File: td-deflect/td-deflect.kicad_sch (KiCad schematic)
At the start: 94 parts, among them J10 Conn_01x02_Male, J11 Conn_01x02_Male, Q1 BSZ42DN25NS3GATMA1, Q10 IPD50R380CE, Q11 IPD50R380CE, Q2 G3R450MT17J, Q3 BSZ42DN25NS3GATMA1, Q4 BCP56, Q5 BCP53, Q6 BD139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

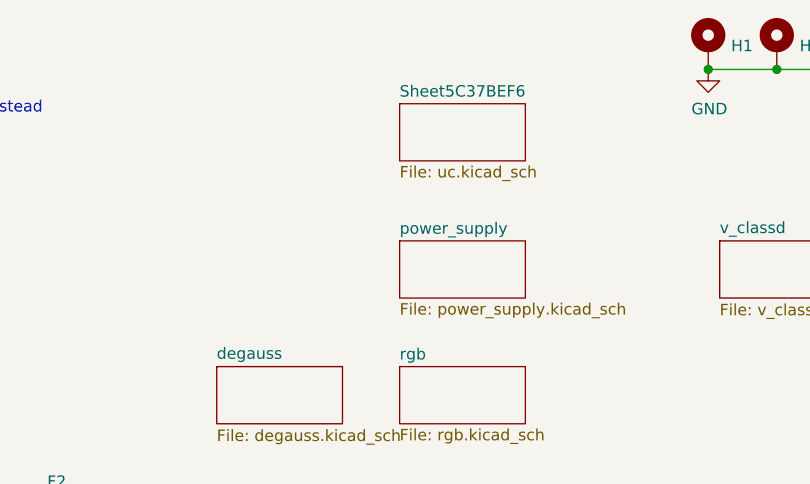
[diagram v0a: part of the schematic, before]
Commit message: update kicad format and move flyback to separate sheet
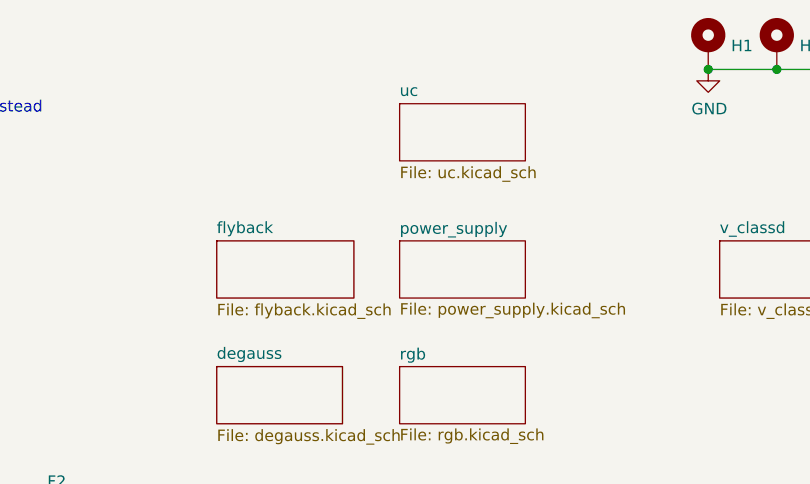
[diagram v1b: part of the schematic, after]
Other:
- sheet Sheet5C37BEF6 renamed uc
- added sheet flyback (flyback.kicad_sch)
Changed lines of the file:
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@@
-(kicad_sch (version 20221206) (generator eeschema)
+(kicad_sch (version 20230121) (generator eeschema)
   (paper "A4")
   (junction (at 35.56 160.02) (diameter 1.016) (color 0 0 0 0)
@@
     (stroke (width 0) (type solid))
     (fill (color 0 0 0 0.0000))
-    (property "Sheetname" "Sheet5C37BEF6" (at 217.17 28.5745 0)
+    (property "Sheetname" "uc" (at 217.17 28.4984 0)
       (effects (font (size 1.27 1.27)) (justify left bottom))
     )
-    (property "Sheetfile" "uc.kicad_sch" (at 217.17 36.0685 0)
+    (property "Sheetfile" "uc.kicad_sch" (at 217.17 36.1446 0)
       (effects (font (size 1.27 1.27)) (justify left top))
     )
@@
       )
     )
+  )
+  (sheet (at 196.85 44.45) (size 15.24 6.35) (fields_autoplaced)
+    (stroke (width 0.1524) (type solid))
+    (fill (color 0 0 0 0.0000))
+    (property "Sheetname" "flyback" (at 196.85 43.7384 0)
+      (effects (font (size 1.27 1.27)) (justify left bottom))
+    )
+    (property "Sheetfile" "flyback.kicad_sch" (at 196.85 51.3846 0)
+      (effects (font (size 1.27 1.27)) (justify left top))
+    )
+    (property "Field2" "" (at 196.85 44.45 0)
+      (effects (font (size 1.27 1.27)) hide)
+    )
+    (instances
+      (project "td-deflect"
+        (path "/55a1a5e1-4d11-4c3e-b2b4-b9d50ddc5f9d" (page "7"))
+      )
+    )

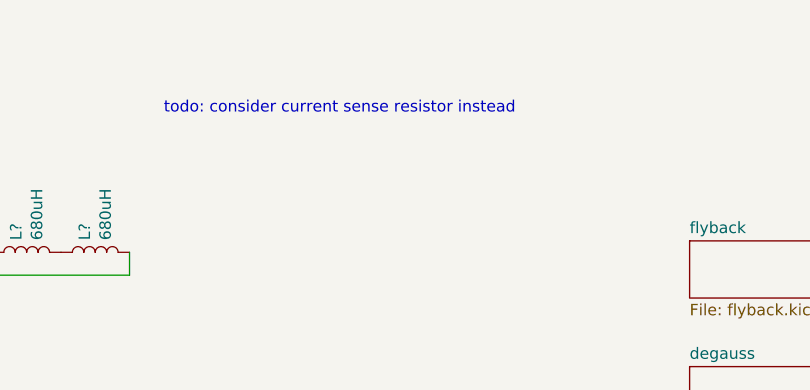
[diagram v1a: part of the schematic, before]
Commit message: drop current sense note
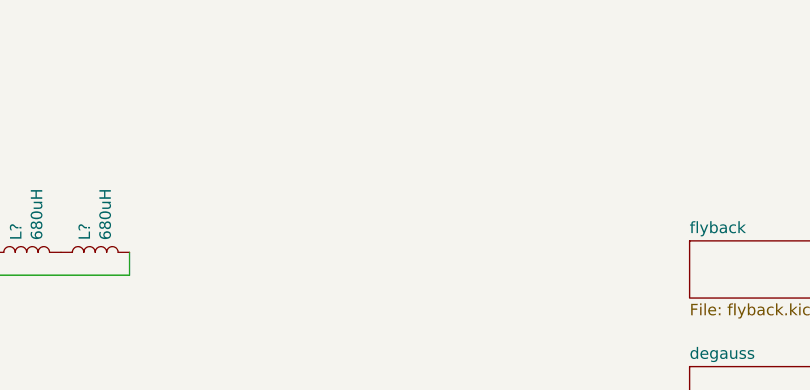
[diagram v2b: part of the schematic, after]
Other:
- note removed: "todo: consider current sense resistor instead"
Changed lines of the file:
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@@
-    (effects (font (size 1.27 1.27)) (justify left bottom))
-  )
-  (text "todo: consider current sense resistor instead" (at 138.43 30.48 0)
     (effects (font (size 1.27 1.27)) (justify left bottom))
   )

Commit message: more updates
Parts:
- added TP1, TP2, TP3: TestPoint, TestPoint:TestPoint_Keystone_5010-5014_Multipurpose, symbol Connector:TestPoint
- C59: renamed from C?; footprint (none) -> Capacitor_SMD:C_0805_2012Metric_Pad1.15x1.40mm_HandSolder
- C69: renamed from C?; footprint (none) -> Capacitor_SMD:CP_Elec_8x11.9; symbol Device:C -> Device:C_Polarized; Digikey (none) -> 493-4571-1-ND
- R67, R68, R70, R71: renamed from R?; footprint (none) -> Resistor_SMD:R_0805_2012Metric_Pad1.15x1.40mm_HandSolder
- gave numbers to parts that had none: 20
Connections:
- net HOT_CURRENT: now also TP2.1
- net HOT_VOLTAGE: now also TP1.1
- net V_CURRENT: now also TP3.1

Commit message: even more updates
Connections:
- net GND: no longer Q2.2 (DS)
- net HOT_CURRENT: now also Q2.2 (DS)
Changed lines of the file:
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@@
   (junction (at 251.46 25.4) (diameter 1.016) (color 0 0 0 0)
   )
-  (junction (at 68.58 88.9) (diameter 0) (color 0 0 0 0)
-  )
   (junction (at 266.7 25.4) (diameter 1.016) (color 0 0 0 0)
   )
@@
   (junction (at 228.6 93.98) (diameter 1.016) (color 0 0 0 0)
   )
+  (junction (at 81.28 86.36) (diameter 0) (color 0 0 0 0)
+  )
   (junction (at 62.23 162.56) (diameter 1.016) (color 0 0 0 0)
   )
@@
     (stroke (width 0) (type solid))
   )
+  (wire (pts (xy 78.74 86.36) (xy 81.28 86.36))
+    (stroke (width 0) (type default))
+  )
   (wire (pts (xy 228.6 93.98) (xy 232.41 93.98))
     (stroke (width 0) (type solid))
@@
     (stroke (width 0) (type solid))
   )
-  (wire (pts (xy 78.74 83.82) (xy 78.74 88.9))
-    (stroke (width 0) (type default))
-  )
   (wire (pts (xy 54.61 170.18) (xy 39.37 170.18))
     (stroke (width 0) (type solid))
@@
     (stroke (width 0) (type solid))
   )
+  (wire (pts (xy 78.74 83.82) (xy 78.74 86.36))
+    (stroke (width 0) (type default))
+  )
   (wire (pts (xy 248.92 93.98) (xy 248.92 119.38))
     (stroke (width 0) (type default))
@@
     (stroke (width 0) (type solid))
   )
-  (wire (pts (xy 78.74 88.9) (xy 68.58 88.9))
-    (stroke (width 0) (type default))
-  )
   (wire (pts (xy 246.38 93.98) (xy 246.38 92.71))

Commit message: small bugfix
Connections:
- net +3V3: no longer R1.1
- new net +3.3VA: R1.1
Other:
- note added: "check output voltage limits"
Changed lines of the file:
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@@
     (stroke (width 0) (type solid))
   )
+  (wire (pts (xy 54.61 149.86) (xy 54.61 162.56))
+    (stroke (width 0) (type solid))
+  )
   (wire (pts (xy 220.98 88.9) (xy 220.98 111.76))
     (stroke (width 0) (type solid))
@@
     (effects (font (size 1.27 1.27)) (justify left bottom))
   )
+  (text "check output voltage limits" (at 95.25 177.8 0)
+    (effects (font (size 1.27 1.27)) (justify left bottom))
+  )
   (text "todo: cooling?" (at 185.42 133.35 0)
     (effects (font (size 1.27 1.27)) (justify left bottom))
@@
     (effects (font (size 1.27 1.27)) (justify left bottom))
   )
-  (label "virtual_ground" (at 273.05 129.54 0) (fields_autoplaced)
-    (effects (font (size 1.27 1.27)) (justify left bottom))
-  )
   (global_label "HOT_IN" (shape input) (at 44.45 81.28 180) (fields_autoplaced)
     (effects (font (size 1.27 1.27)) (justify right))
@@
     )
   )
-  (global_label "virtual_ground" (shape input) (at 54.61 149.86 180) (fields_autoplaced)
-    (effects (font (size 1.27 1.27)) (justify right))
-    (property "Intersheetrefs" "${INTERSHEET_REFS}" (at 38.7391 149.9394 0)
-      (effects (font (size 1.27 1.27)) (justify right) hide)
+  (global_label "virtual_ground" (shape input) (at 273.05 129.54 0) (fields_autoplaced)
+    (effects (font (size 1.27 1.27)) (justify left))
+    (property "Intersheetrefs" "${INTERSHEET_REFS}" (at 288.9209 129.4606 0)
+      (effects (font (size 1.27 1.27)) (justify left) hide)
     )
   )
@@
     )
   )
-  (symbol (lib_id "power:+3.3V") (at 35.56 152.4 0) (unit 1)
-    (in_bom yes) (on_board yes) (dnp no)
-    (property "Reference" "#PWR0159" (at 35.56 156.21 0)
-      (effects (font (size 1.27 1.27)) hide)
-    )
-    (property "Value" "+3.3V" (at 35.941 148.0058 0)
-      (effects (font (size 1.27 1.27)))
-    )
-    (property "Footprint" "" (at 35.56 152.4 0)
-      (effects (font (size 1.27 1.27)) hide)
-    )
-    (property "Datasheet" "" (at 35.56 152.4 0)
-      (effects (font (size 1.27 1.27)) hide)
-    )
-    (pin "1")
-    (instances
-      (project "td-deflect"
-        (path "/55a1a5e1-4d11-4c3e-b2b4-b9d50ddc5f9d"
-          (reference "#PWR0159") (unit 1)
-        )
-      )
-    )
-  )
   (symbol (lib_id "Device:R") (at 54.61 146.05 0) (unit 1)
     (in_bom yes) (on_board yes) (dnp no)
@@
         )
       )
+    )
+  )
+  (symbol (lib_id "power:+3.3VA") (at 35.56 152.4 0) (unit 1)
+    (in_bom yes) (on_board yes) (dnp no) (fields_autoplaced)
+    (property "Reference" "#PWR010" (at 35.56 156.21 0)
+      (effects (font (size 1.27 1.27)) hide)
+    )
+    (property "Value" "+3.3VA" (at 35.56 148.8981 0)
+      (effects (font (size 1.27 1.27)))
+    )
+    (property "Footprint" "" (at 35.56 152.4 0)
+      (effects (font (size 1.27 1.27)) hide)
+    )
+    (property "Datasheet" "" (at 35.56 152.4 0)
+      (effects (font (size 1.27 1.27)) hide)
+    )
+    (pin "1")
+    (instances
+      (project "td-deflect"
+        (path "/55a1a5e1-4d11-4c3e-b2b4-b9d50ddc5f9d/00000000-0000-0000-0000-00005c37bef7"
+          (reference "#PWR010") (unit 1)
+        )
+        (path "/55a1a5e1-4d11-4c3e-b2b4-b9d50ddc5f9d"
+          (reference "#PWR045") (unit 1)
+        )
+      )

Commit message: switch to new 0805 footprint
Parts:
- C1, C10, C12, C2, C3, C4, C5, C59, C60, C68, C7, C8, C9: footprint Capacitor_SMD:C_0805_2012Metric_Pad1.15x1.40mm_HandSolder -> Capacitor_SMD:C_0805_2012Metric_Pad1.18x1.45mm_HandSolder
- R1, R10, R11, R15, R16, R17, R18, R2, R20, R21, R3, R4, R5, R64, R65, R67, R68, R7, R70, R71, R72, R8, R9: footprint Resistor_SMD:R_0805_2012Metric_Pad1.15x1.40mm_HandSolder -> Resistor_SMD:R_0805_2012Metric_Pad1.20x1.40mm_HandSolder
- R23, R24, R25, R26, R27, R28: footprint Resistor_SMD:R_1206_3216Metric_Pad1.42x1.75mm_HandSolder -> Resistor_SMD:R_1206_3216Metric_Pad1.30x1.75mm_HandSolder

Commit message: use off board bplus h supply
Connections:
- net HT: no longer Q1.5 (D)
- new net +3.3V: Q1.5 (D)
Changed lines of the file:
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@@
     (stroke (width 0) (type default))
   )
-  (wire (pts (xy 87.63 30.48) (xy 87.63 28.575))
+  (wire (pts (xy 87.63 27.94) (xy 87.63 30.48))
     (stroke (width 0) (type solid))
   )
@@
     )
   )
-  (symbol (lib_id "power:HT") (at 87.63 28.575 0) (unit 1)
-    (in_bom yes) (on_board yes) (dnp no)
-    (property "Reference" "#PWR0123" (at 87.63 25.527 0)
-      (effects (font (size 1.27 1.27)) hide)
-    )
-    (property "Value" "HT" (at 88.138 24.9428 0)
-      (effects (font (size 1.27 1.27)))
-    )
-    (property "Footprint" "" (at 87.63 28.575 0)
-      (effects (font (size 1.27 1.27)) hide)
-    )
-    (property "Datasheet" "" (at 87.63 28.575 0)
-      (effects (font (size 1.27 1.27)) hide)
-    )
-    (pin "1")
-    (instances
-      (project "td-deflect"
-        (path "/55a1a5e1-4d11-4c3e-b2b4-b9d50ddc5f9d"
-          (reference "#PWR0123") (unit 1)
-        )
-      )
-    )
-  )
   (symbol (lib_id "power:GND") (at 87.63 55.88 0) (unit 1)
     (in_bom yes) (on_board yes) (dnp no)
@@
         )
       )
+    )
+  )
+  (symbol (lib_id "td-crt:B+H") (at 87.63 27.94 0) (unit 1)
+    (in_bom yes) (on_board yes) (dnp no) (fields_autoplaced)
+    (property "Reference" "#PWR010" (at 87.63 31.75 0)
+      (effects (font (size 1.27 1.27)) hide)
+    )
+    (property "Value" "B+H" (at 87.63 23.8069 0)
+      (effects (font (size 1.27 1.27)))
+    )
+    (property "Footprint" "" (at 87.63 27.94 0)
+      (effects (font (size 1.27 1.27)) hide)
+    )
+    (property "Datasheet" "" (at 87.63 27.94 0)
+      (effects (font (size 1.27 1.27)) hide)
+    )
+    (pin "1")
+    (instances
+      (project "td-deflect"
+        (path "/55a1a5e1-4d11-4c3e-b2b4-b9d50ddc5f9d"
+          (reference "#PWR010") (unit 1)
+        )
+      )

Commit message: update part numbers
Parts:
- C59: value C -> 0.1uF; Digikey (none) -> 445-8899-1-ND
- Q1, Q3: value BSZ42DN25NS3GATMA1 -> BSC600N25NS3GATMA1CT-ND; Digikey BSZ42DN25NS3GATMA1CT-ND -> BSC600N25NS3GATMA1CT-ND
- Q6: value BD139 -> 2SC4382; Digikey 497-12750-5-ND -> 2SC4382-ND
- Q7: value BD140 -> 2SA1668; Digikey 497-14760-5-ND -> 2SA1668-ND
- U31: Digikey (none) -> 445-8899-1-ND
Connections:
- net HT is gone; now on net +3.3V: C59.1
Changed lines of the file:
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@@
       (effects (font (size 1.27 1.27)) (justify left))
     )
-    (property "Value" "BD140" (at 148.3868 136.017 0)
+    (property "Value" "2SA1668" (at 148.3868 136.017 0)
       (effects (font (size 1.27 1.27)) (justify left))
     )
@@
       (effects (font (size 1.27 1.27)) (justify left) hide)
     )
-    (property "Digikey" " 497-14760-5-ND " (at 143.51 137.16 0)
+    (property "Digikey" "2SA1668-ND" (at 143.51 137.16 0)
       (effects (font (size 1.27 1.27)) hide)
     )
@@
       (effects (font (size 1.27 1.27)) (justify left))
     )
-    (property "Value" "BD139" (at 148.3868 173.863 0)
+    (property "Value" "2SC4382" (at 148.3868 173.863 0)
       (effects (font (size 1.27 1.27)) (justify left))
     )
@@
       (effects (font (size 1.27 1.27)) (justify left) hide)
     )
-    (property "Digikey" " 497-12750-5-ND " (at 143.51 172.72 0)
+    (property "Digikey" "2SC4382-ND" (at 143.51 172.72 0)
       (effects (font (size 1.27 1.27)) hide)
     )
@@
       (effects (font (size 1.27 1.27)) (justify left))
     )
-    (property "Value" "BSZ42DN25NS3GATMA1" (at 90.2716 36.703 0)
+    (property "Value" "BSC600N25NS3GATMA1CT-ND" (at 90.2716 36.703 0)
       (effects (font (size 1.27 1.27)) (justify left))
     )
@@
       (effects (font (size 1.27 1.27)) (justify left) hide)
     )
-    (property "Digikey" "BSZ42DN25NS3GATMA1CT-ND" (at 85.09 35.56 0)
+    (property "Digikey" "BSC600N25NS3GATMA1CT-ND" (at 85.09 35.56 0)
       (effects (font (size 1.27 1.27)) hide)
     )
@@
       (effects (font (size 1.27 1.27)) (justify left))
     )
-    (property "Value" "BSZ42DN25NS3GATMA1" (at 90.2716 51.943 0)
+    (property "Value" "BSC600N25NS3GATMA1CT-ND" (at 90.2716 51.943 0)
       (effects (font (size 1.27 1.27)) (justify left))
     )
@@
       (effects (font (size 1.27 1.27)) (justify left) hide)
     )
-    (property "Digikey" "BSZ42DN25NS3GATMA1CT-ND" (at 85.09 50.8 0)
+    (property "Digikey" "BSC600N25NS3GATMA1CT-ND" (at 85.09 50.8 0)
       (effects (font (size 1.27 1.27)) hide)
     )
@@
     (property "Datasheet" "https://docs.broadcom.com/docs/AV02-0173EN" (at 191.77 147.32 0)
       (effects (font (size 1.27 1.27)) (justify left) hide)
+    )
+    (property "Digikey" "445-8899-1-ND" (at 191.77 147.32 90)
+      (effects (font (size 1.27 1.27)) hide)
     )
     (pin "1")
@@
     )
   )
-  (symbol (lib_id "power:HT") (at 26.67 39.37 0) (unit 1)
-    (in_bom yes) (on_board yes) (dnp no)
-    (property "Reference" "#PWR0160" (at 26.67 36.322 0)
-      (effects (font (size 1.27 1.27)) hide)
-    )
-    (property "Value" "HT" (at 27.178 35.7378 0)
-      (effects (font (size 1.27 1.27)))
-    )
-    (property "Footprint" "" (at 26.67 39.37 0)
-      (effects (font (size 1.27 1.27)) hide)
-    )
-    (property "Datasheet" "" (at 26.67 39.37 0)
-      (effects (font (size 1.27 1.27)) hide)
-    )
-    (pin "1")
-    (instances
-      (project "td-deflect"
-        (path "/55a1a5e1-4d11-4c3e-b2b4-b9d50ddc5f9d"
-          (reference "#PWR0160") (unit 1)
-        )
-      )
-    )
-  )
   (symbol (lib_id "td-crt:B+H") (at 87.63 27.94 0) (unit 1)
     (in_bom yes) (on_board yes) (dnp no) (fields_autoplaced)
@@
       (effects (font (size 1.27 1.27)) (justify left))
     )
-    (property "Value" "C" (at 30.48 44.4499 0)
+    (property "Value" "0.1uF" (at 30.48 44.4499 0)
       (effects (font (size 1.27 1.27)) (justify left))
     )
@@
       (effects (font (size 1.27 1.27)) hide)
     )
+    (property "Digikey" "445-8899-1-ND" (at 26.67 43.18 0)
+      (effects (font (size 1.27 1.27)) hide)
+    )
     (pin "1")
     (pin "2")
@@
         )
       )
+    )
+  )
+  (symbol (lib_id "td-crt:B+H") (at 26.67 39.37 0) (unit 1)
+    (in_bom yes) (on_board yes) (dnp no) (fields_autoplaced)
+    (property "Reference" "#PWR07" (at 26.67 43.18 0)
+      (effects (font (size 1.27 1.27)) hide)
+    )
+    (property "Value" "B+H" (at 26.67 35.2369 0)
+      (effects (font (size 1.27 1.27)))
+    )
+    (property "Footprint" "" (at 26.67 39.37 0)
+      (effects (font (size 1.27 1.27)) hide)
+    )
+    (property "Datasheet" "" (at 26.67 39.37 0)
+      (effects (font (size 1.27 1.27)) hide)
+    )
+    (pin "1")
+    (instances
+      (project "td-deflect"
+        (path "/55a1a5e1-4d11-4c3e-b2b4-b9d50ddc5f9d"
+          (reference "#PWR07") (unit 1)
+        )
+      )
